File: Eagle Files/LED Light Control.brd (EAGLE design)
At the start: 49.2 x 80 mm, 23 parts, among them IC1 LM317MBSTT3, X2 TERMINAL-BLOCK-3.5MM-2-PIN-RO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, X3 TERMINAL-BLOCK-3.5MM-3-PIN-RO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

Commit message: Changes
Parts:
- removed X2: TERMINAL-BLOCK-3.5MM-2-PIN-ROUND-PAD, Rembrandt Electronics - Terminal Block 3-5mm v1-0:TERMINAL-BLOCK-2-PIN-3.5MM-ROUND-PAD
- added CN1: (no value), adafruit:DCJACK_2MM_PTH
- moved C3 8.89 mm to (43.2, 2.54)
- moved R8 8.89 mm to (34.3, 11.4)
- moved X3 8.89 mm to (34.3, 3.81)
- moved R10 8.89 mm to (39.4, 11.4)
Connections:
- new net GNDBREAK: CN1.GNDBREAK
- net +5V: now also CN1.PWR; no longer X2.1
- net GND: now also CN1.GND; no longer X2.2
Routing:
- net +5V: track 59.1 -> 70.5 mm, vias 1 -> 2
- net 5VDATA: track 11.8 -> 16.8 mm
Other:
- board text added: "LehmanCreations.com/LEDController"
- board text removed: "LehmanCreations.com/LEDControl"

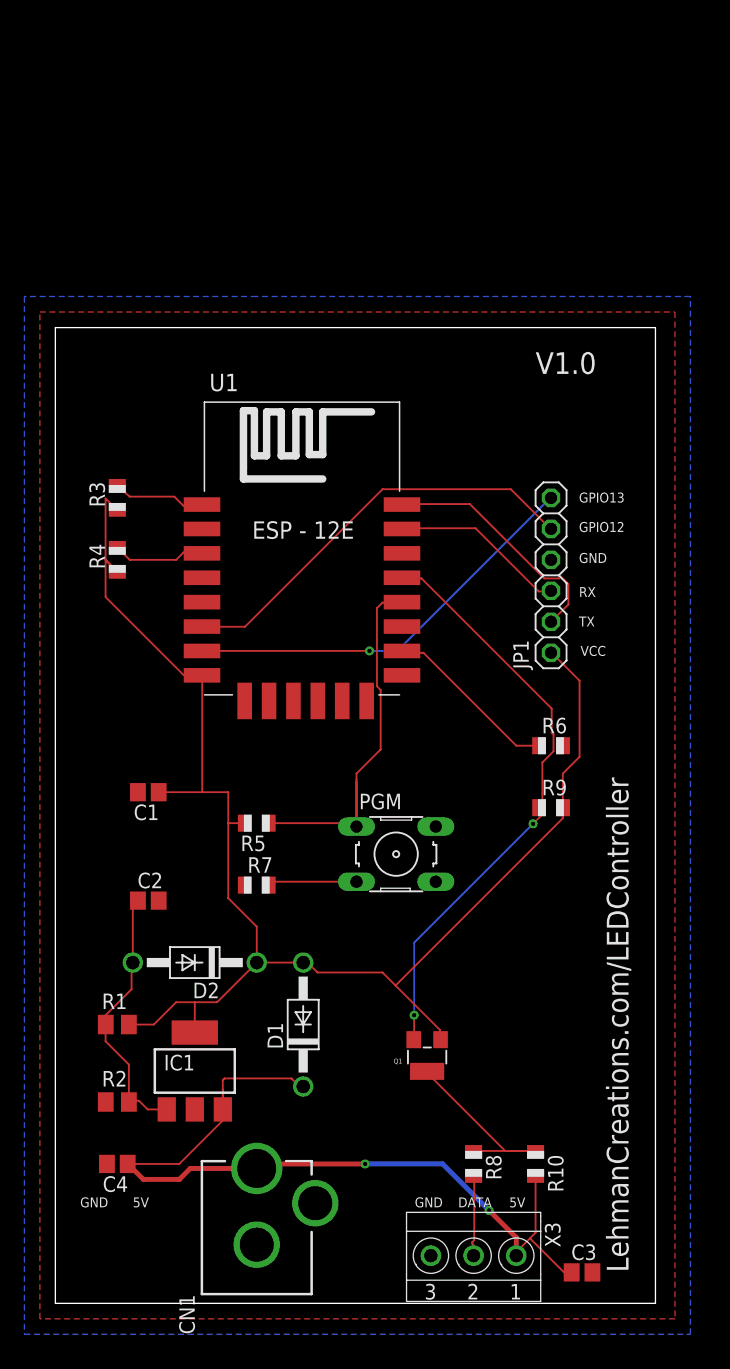
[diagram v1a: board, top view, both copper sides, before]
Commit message: Complete redisign of board. Also changed out the regulator on the schematic for a new one
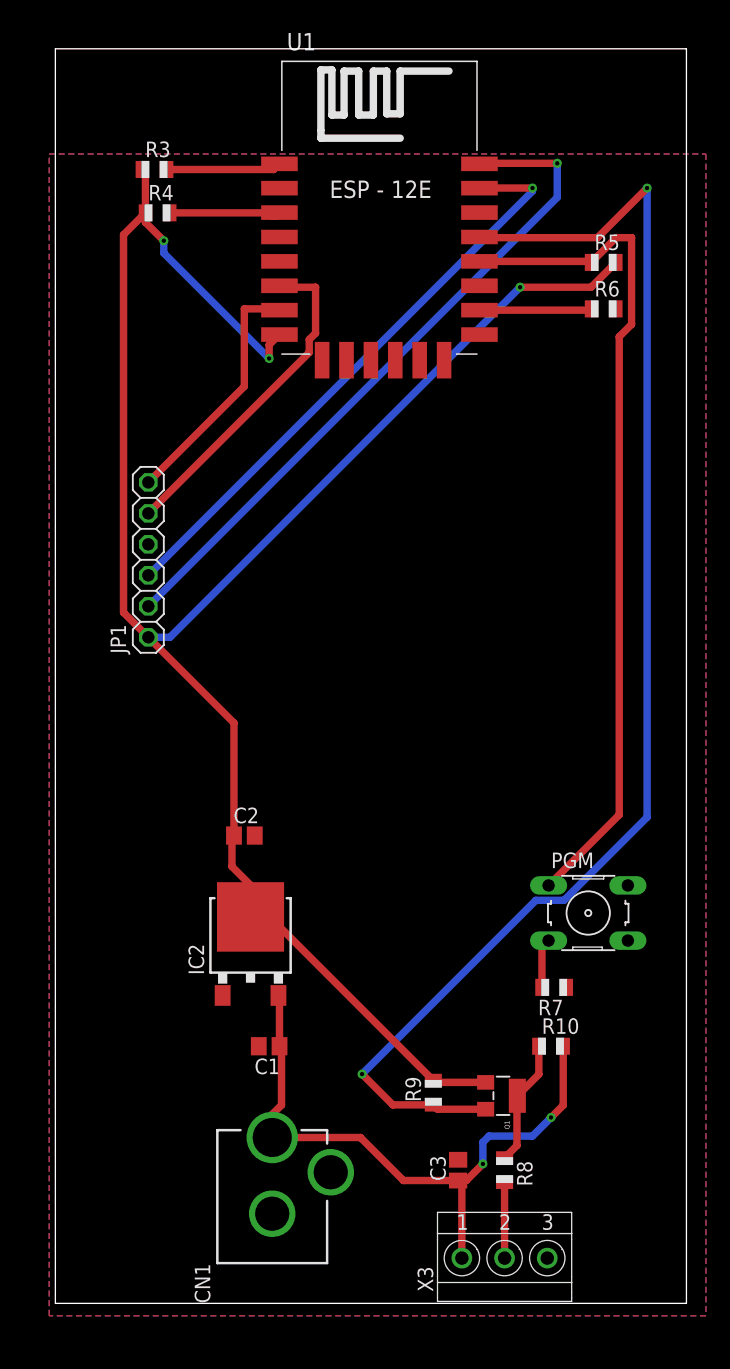
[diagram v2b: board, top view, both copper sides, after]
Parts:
- removed C4: .01uF, adafruit:C0805
- removed D1, D2: 1N4002, diode:DO41-10
- removed IC1: LM317MBSTT3, v-reg:SOT223
- removed R1: 240Ω, resistor:M0805
- removed R2: 394Ω, resistor:M0805
- added IC2: LM1117DT-3.3, lm1117:TO252
- C1: value 1uF -> 100uF
- C2: value 10uF -> 100uF
- moved R5 54.1 mm to (45.0, 85.3), turned to 0 degrees
- moved R6 36.1 mm to (45.0, 81.5)
- moved JP1 33.0 mm to (7.62, 61.0)
- moved U1 28.7 mm to (26.7, 87.6)
- moved R4 28.6 mm to (8.38, 89.4), turned to 0 degrees
- moved R3 27.1 mm to (8.13, 93.0), turned to 0 degrees
- moved R7 25.8 mm to (40.9, 25.9), turned to 180 degrees
- moved R9 25.3 mm to (31.0, 17.3), turned to 90 degrees
- moved C1 23.1 mm to (17.5, 21.1)
- moved PGM 16.5 mm to (43.7, 32.0)
- moved C3 13.2 mm to (33.0, 10.9), turned to 90 degrees
- moved R10 9.74 mm to (40.6, 21.1), turned to 0 degrees
- moved C2 9.51 mm to (15.5, 38.4)
- moved Q1 6.93 mm to (36.6, 17.0), turned to 270 degrees
- moved CN1 2.84 mm to (17.8, 0.00)
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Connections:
- removed net N$1: C2.1, D2.A, IC1.1, R1.1, R2.2
- net +5V: now also C1.1, IC2.2; no longer C4.1, D1.C, IC1.3
- net GND: now also IC2.1; no longer C4.2, R2.1
- net VCC: now also C2.1, IC2.3; no longer C1.1, D1.A, D2.C, IC1.4, R1.2
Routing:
- net DATA: track 48.8 -> 110.9 mm
- net VCC: track 122.5 -> 162.4 mm, vias 0 -> 3
- net N$9: track 32.0 -> 69.3 mm
- net TX: track 20.2 -> 56.6 mm, vias 0 -> 1
- net RX: track 14.4 -> 49.1 mm, vias 0 -> 1
- net N$1: track 22.1 -> 0.00 mm
- net +5V: track 70.5 -> 52.3 mm
- net GPIO13: track 33.8 -> 20.4 mm, vias 1 -> 0
- net GPIO12: track 34.6 -> 27.4 mm
- net 5VDATA: track 16.8 -> 10.3 mm
- net N$5: track 14.5 -> 9.23 mm
- net N$6: track 7.35 -> 4.06 mm
- net N$2: track 7.64 -> 9.44 mm
- net N$3: track 7.62 -> 9.21 mm
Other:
- board size 49.2 x 80 mm -> 51.7 x 102.9 mm
- board text removed: "5V"
- board text removed: "DATA"
- board text removed: "For use with Neopixel light strips or other 5V WS2812 LED"
- board text removed: "GND"
- board text removed: "GPIO12"
- board text removed: "GPIO13"
- board text removed: "LehmanCreations.com/LEDController"
- board text removed: "RX"
- board text removed: "TX"
- board text removed: "V1.0"
- board text removed: "VCC"

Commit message: Made board smaller and added lables
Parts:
- moved R6 14.5 mm to (45.0, 67.1)
- moved JP1 14.5 mm to (7.62, 46.5)
- moved R3 14.5 mm to (8.13, 78.5)
- moved R4 14.5 mm to (8.38, 74.9)
- moved R5 14.5 mm to (45.0, 70.9)
- moved U1 14.5 mm to (26.7, 73.2)
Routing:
- net N$9: track 69.3 -> 54.8 mm
- net DATA: track 110.9 -> 96.5 mm
- net VCC: track 162.4 -> 151.0 mm
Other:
- board size 51.7 x 102.9 mm -> 52.5 x 88.1 mm
- board text added: "5V"
- board text added: "D"
- board text added: "GND"
- board text added: "GPIO12"
- board text added: "GPIO13"
- board text added: "LehmanCreations.com/ledcontroller"
- board text added: "REV 1"
- board text added: "RX"
- board text added: "TX"
- board text added: "VCC"

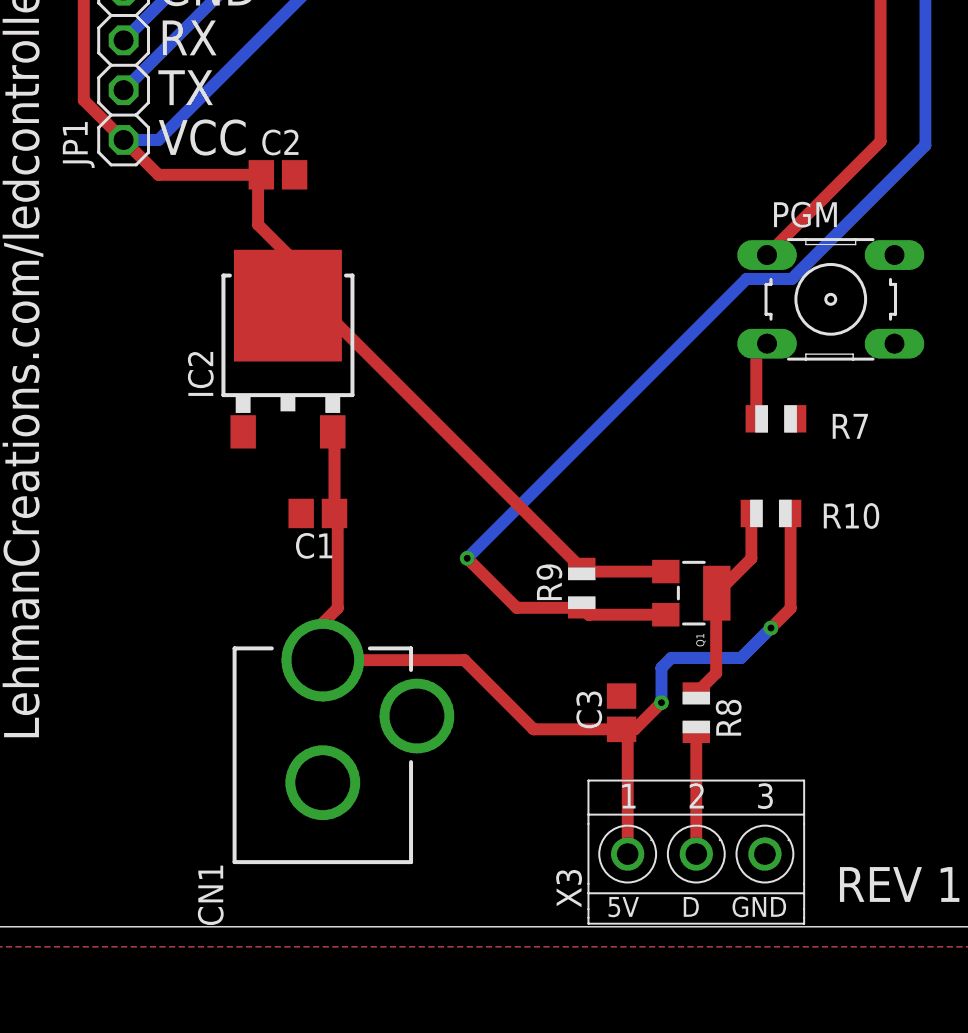
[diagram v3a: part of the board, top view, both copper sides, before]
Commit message: Made board smaller
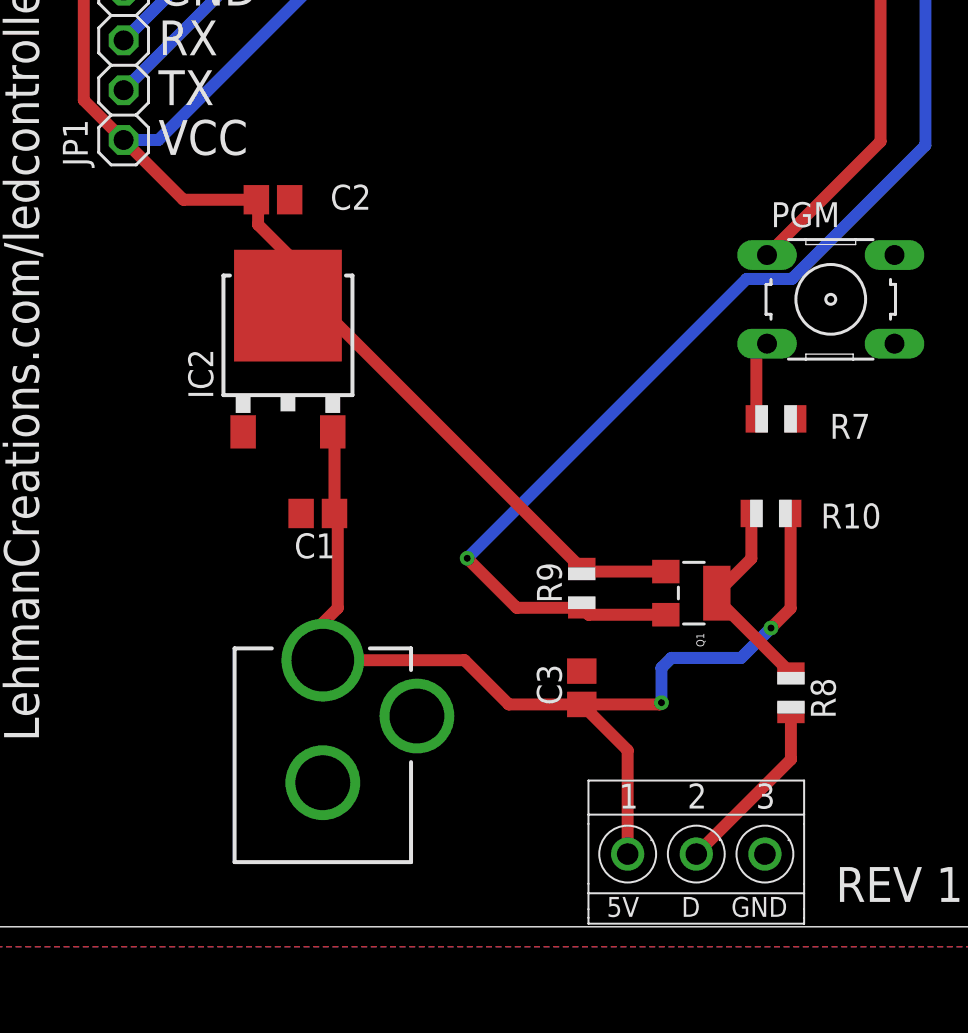
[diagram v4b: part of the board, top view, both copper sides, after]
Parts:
- moved R8 4.93 mm to (41.7, 11.9)
- moved C3 2.40 mm to (31.0, 12.2)
- moved C2 1.30 mm to (15.2, 37.1)
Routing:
- net N$7: track 6.21 -> 9.23 mm
- net +5V: track 52.3 -> 53.4 mm
- net VCC: track 151.0 -> 150.0 mm
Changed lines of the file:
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@@
 <wire x1="51.994" y1="88.128" x2="-0.254" y2="88.128" width="0" layer="20"/>
 <wire x1="-0.254" y1="88.128" x2="-0.508" y2="0" width="0" layer="20"/>
-<dimension x1="51.74" y1="110.48" x2="0" y2="110.48" x3="25.87" y3="107.15" textsize="1.778" layer="51" dtype="horizontal" unit="inch" visible="yes"/>
-<dimension x1="51.74" y1="0" x2="51.74" y2="102.86" x3="62.23" y3="51.43" textsize="1.778" layer="51" dtype="horizontal" unit="inch" visible="yes"/>
 <text x="9.398" y="39.37" size="1.778" layer="25">VCC</text>
 <text x="9.398" y="41.91" size="1.778" layer="25">TX</text>
@@
 </autorouter>
 <elements>
-<element name="C3" library="adafruit" package="C0805" value="1000uF" x="33.02" y="10.922" rot="R90"/>
+<element name="C3" library="adafruit" package="C0805" value="1000uF" x="30.988" y="12.192" rot="R90"/>
 <element name="CN1" library="adafruit" package="DCJACK_2MM_PTH" value="" x="17.78" y="0" smashed="yes">
-<attribute name="NAME" x="12.7" y="0" size="1.27" layer="25" rot="R90"/>
 <attribute name="VALUE" x="24.13" y="0" size="1.27" layer="27" rot="R90"/>
 </element>
@@
 <attribute name="VALUE" x="41.656" y="28.194" size="1.27" layer="27" rot="R180"/>
 </element>
-<element name="R8" library="adafruit" package="R0805" value="300Ω" x="36.83" y="10.922" rot="R270"/>
+<element name="R8" library="adafruit" package="R0805" value="300Ω" x="41.656" y="11.938" rot="R270"/>
 <element name="R9" library="adafruit" package="R0805" value="10K" x="30.988" y="17.272" rot="R90"/>
 <element name="U1" library="esp8266modules" package="ESP12E-SMD" value="" x="26.67" y="73.152"/>
 <element name="X3" library="Rembrandt Electronics - Terminal Block 3-5mm v1-0" package="TERMINAL-BLOCK-3-PIN-3.5MM-ROUND-PAD" value="TERMINAL-BLOCK-3.5MM-3-PIN-ROUND-PAD" x="36.83" y="3.81" smashed="yes">
-<attribute name="NAME" x="30.975" y="0.9525" size="1.27" layer="25" rot="R90"/>
 <attribute name="VALUE" x="33.0275" y="7.9375" size="1.27" layer="27"/>
 </element>
@@
 </element>
 <element name="C1" library="adafruit" package="C0805" value="100uF" x="17.526" y="21.082" rot="R180"/>
-<element name="C2" library="adafruit" package="C0805" value="100uF" x="15.494" y="38.354"/>
+<element name="C2" library="adafruit" package="C0805" value="100uF" x="15.24" y="37.084" smashed="yes">
+<attribute name="NAME" x="18.161" y="36.576" size="1.27" layer="25"/>
+<attribute name="VALUE" x="14.351" y="34.798" size="1.27" layer="27"/>
+</element>
 </elements>
 <signals>
@@
 <wire x1="16.002" y1="31.684" x2="16.002" y2="34.29" width="0.6096" layer="1"/>
 <wire x1="16.002" y1="34.29" x2="14.478" y2="35.814" width="0.6096" layer="1"/>
-<wire x1="14.478" y1="35.814" x2="14.478" y2="38.188" width="0.6096" layer="1"/>
-<wire x1="14.478" y1="38.188" x2="14.644" y2="38.354" width="0.6096" layer="1"/>
-<wire x1="9.398" y1="38.354" x2="7.62" y2="40.132" width="0.6096" layer="1"/>
+<wire x1="14.478" y1="35.814" x2="14.478" y2="36.996" width="0.6096" layer="1"/>
+<wire x1="14.478" y1="36.996" x2="14.39" y2="37.084" width="0.6096" layer="1"/>
+<wire x1="10.668" y1="37.084" x2="7.62" y2="40.132" width="0.6096" layer="1"/>
 <wire x1="7.62" y1="40.132" x2="5.588" y2="42.164" width="0.6096" layer="1"/>
 <wire x1="5.588" y1="73.136" x2="7.382" y2="74.93" width="0.6096" layer="1"/>
@@
 <wire x1="38.1" y1="68.834" x2="9.398" y2="40.132" width="0.6096" layer="16"/>
 <wire x1="9.398" y1="40.132" x2="7.62" y2="40.132" width="0.6096" layer="16"/>
-<wire x1="14.644" y1="38.354" x2="9.398" y2="38.354" width="0.6096" layer="1"/>
+<wire x1="14.39" y1="37.084" x2="10.668" y2="37.084" width="0.6096" layer="1"/>
 </signal>
 <signal name="N$6">
@@
 <wire x1="18.376" y1="21.082" x2="18.376" y2="25.155" width="0.6096" layer="1"/>
 <wire x1="18.376" y1="25.155" x2="18.287" y2="25.244" width="0.6096" layer="1"/>
-<wire x1="33.33" y1="3.71" x2="33.33" y2="9.762" width="0.6096" layer="1"/>
-<wire x1="33.33" y1="9.762" x2="33.02" y2="10.072" width="0.6096" layer="1"/>
-<wire x1="33.02" y1="10.072" x2="28.536" y2="10.072" width="0.6096" layer="1"/>
+<wire x1="33.33" y1="3.71" x2="33.33" y2="9" width="0.6096" layer="1"/>
+<wire x1="33.33" y1="9" x2="30.988" y2="11.342" width="0.6096" layer="1"/>
+<wire x1="30.988" y1="11.342" x2="27.266" y2="11.342" width="0.6096" layer="1"/>
 <wire x1="25.008" y1="13.6" x2="17.78" y2="13.6" width="0.6096" layer="1"/>
-<wire x1="28.536" y1="10.072" x2="25.008" y2="13.6" width="0.6096" layer="1"/>
+<wire x1="27.266" y1="11.342" x2="25.008" y2="13.6" width="0.6096" layer="1"/>
 <wire x1="41.64" y1="21.082" x2="41.64" y2="16.24" width="0.6096" layer="1"/>
 <wire x1="41.64" y1="16.24" x2="40.64" y2="15.24" width="0.6096" layer="1"/>
@@
 <wire x1="35.052" y1="13.208" x2="35.052" y2="11.43" width="0.6096" layer="16"/>
 <via x="35.052" y="11.43" extent="1-16" drill="0.35"/>
-<wire x1="35.052" y1="11.43" x2="33.694" y2="10.072" width="0.6096" layer="1"/>
-<wire x1="33.694" y1="10.072" x2="33.02" y2="10.072" width="0.6096" layer="1"/>
+<wire x1="34.964" y1="11.342" x2="30.988" y2="11.342" width="0.6096" layer="1"/>
+<wire x1="35.052" y1="11.43" x2="34.964" y2="11.342" width="0.6096" layer="1"/>
 </signal>
 <signal name="5VDATA">
@@
 <contactref element="Q1" pad="3"/>
 <contactref element="R10" pad="1"/>
-<wire x1="36.83" y1="11.922" x2="37.846" y2="12.938" width="0.6096" layer="1"/>
-<wire x1="37.846" y1="12.938" x2="37.846" y2="16.51" width="0.6096" layer="1"/>
-<wire x1="37.846" y1="16.51" x2="37.876" y2="16.54" width="0.6096" layer="1"/>
-<wire x1="37.876" y1="16.54" x2="37.876" y2="17.018" width="0.6096" layer="1"/>
+<wire x1="41.656" y1="12.938" x2="37.876" y2="16.718" width="0.6096" layer="1"/>
+<wire x1="37.876" y1="16.718" x2="37.876" y2="17.018" width="0.6096" layer="1"/>
 <wire x1="39.64" y1="21.082" x2="39.64" y2="18.782" width="0.6096" layer="1"/>
 <wire x1="39.64" y1="18.782" x2="37.876" y2="17.018" width="0.6096" layer="1"/>
@@
 <contactref element="R8" pad="2"/>
 <contactref element="X3" pad="2"/>
-<wire x1="36.83" y1="9.922" x2="36.83" y2="3.71" width="0.6096" layer="1"/>
+<wire x1="41.656" y1="10.938" x2="41.656" y2="8.536" width="0.6096" layer="1"/>
+<wire x1="41.656" y1="8.536" x2="36.83" y2="3.71" width="0.6096" layer="1"/>
 </signal>
 <signal name="N$2">
